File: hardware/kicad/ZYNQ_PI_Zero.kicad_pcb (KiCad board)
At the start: 6 copper layers, 65 x 30 mm, 111 parts, among them J1 HDMI_C_1.4, J201 Conn_02x05_Odd_Even, J202 Conn_01x04_Pin, J501 Conn_02x20_Counter_Clockwise, J701 USB_C_Receptacle_USB2.0_16P, J702 USB_C_Receptacle_USB2.0_16P, J703 USB_C_Receptacle_USB2.0_16P, J801 Micro_SD_Card, Q201 MMBT3904, U201 xc7z007sclg225, U301 MT41K256M16TW-107_P

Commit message: layout: finish dq0 & dq1 routing
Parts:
- removed C433: 10u, Capacitor_SMD:C_0805_2012Metric
- removed C435, C463, C464: 100n, Capacitor_SMD:C_0402_1005Metric
- removed C438: 100u, Capacitor_SMD:C_1206_3216Metric
- removed C443: 4u7, Capacitor_SMD:C_0603_1608Metric
- removed J1: HDMI_C_1.4, Projects:HDMI-SMD_A71-05H4-111N1
- removed J201: Conn_02x05_Odd_Even, Connector_PinSocket_2.54mm:PinSocket_2x05_P2.54mm_Vertical
- removed J702, J703: USB_C_Receptacle_USB2.0_16P, Connector_USB:USB_C_Receptacle_GCT_USB4105-xx-A_16P_TopMnt_Horizontal
- removed J801: Micro_SD_Card, Projects:TF-SMD_503398-1892
- added C301: 100n, Capacitor_SMD:C_0402_1005Metric, F.Cu at (116.2, 97.2)
- added C302: 100n, Capacitor_SMD:C_0402_1005Metric, F.Cu at (116.2, 98.1)
- added C303: 1u, Capacitor_SMD:C_0603_1608Metric, F.Cu at (105.5, 138.7)
- added C304: 1u, Capacitor_SMD:C_0603_1608Metric, F.Cu at (105.5, 141.2)
- added C305: 1u, Capacitor_SMD:C_0603_1608Metric, F.Cu at (105.5, 143.8)
- added C306: 1u, Capacitor_SMD:C_0603_1608Metric, F.Cu at (105.5, 146.3)
- added C307: 100n, Capacitor_SMD:C_0402_1005Metric, B.Cu at (117.2, 91.4)
- added C308: 1u, Capacitor_SMD:C_0603_1608Metric, F.Cu at (105.5, 148.8)
- added C309: 100n, Capacitor_SMD:C_0402_1005Metric, B.Cu at (118.9, 91.4)
- added C310: 100n, Capacitor_SMD:C_0402_1005Metric, B.Cu at (120.7, 91.4)
- added C311: 100n, Capacitor_SMD:C_0402_1005Metric, B.Cu at (116.3, 103.6)
- added C312: 100n, Capacitor_SMD:C_0402_1005Metric, B.Cu at (116.3, 105.2)
- added C313: 100n, Capacitor_SMD:C_0402_1005Metric, B.Cu at (147.8, 98.0)
- added C314: 100n, Capacitor_SMD:C_0402_1005Metric, B.Cu at (128.0, 105.2)
- added C315: 100n, Capacitor_SMD:C_0402_1005Metric, B.Cu at (116.7, 94.3)
- added C316: 100n, Capacitor_SMD:C_0402_1005Metric, B.Cu at (116.7, 96.0)
- added C317: 100n, Capacitor_SMD:C_0402_1005Metric, B.Cu at (116.7, 97.7)
- added C318: 100n, Capacitor_SMD:C_0402_1005Metric, B.Cu at (128.0, 103.6)
- added C701: 10u, Capacitor_SMD:C_0805_2012Metric, F.Cu at (296.2, 176.7)
- added C702: 100n, Capacitor_SMD:C_0402_1005Metric, F.Cu at (299.9, 176.2)
- added C901: 100n, Capacitor_SMD:C_0402_1005Metric, F.Cu at (267.1, 179.9)
- added D601: SS14, Diode_SMD:D_SMA, F.Cu at (303.0, 149.7)
- added D602: SS14, Diode_SMD:D_SMA, F.Cu at (303.0, 154.2)
- added D801: PL_LED, LED_SMD:LED_0603_1608Metric, F.Cu at (277.7, 172.3)
- added D902: PS_LED, LED_SMD:LED_0603_1608Metric, F.Cu at (267.7, 177.6)
- added F601: Polyfuse, Fuse:Fuse_0603_1608Metric, F.Cu at (296.0, 152.6)
- added FB701: 120OHM@100M, Inductor_SMD:L_0402_1005Metric, F.Cu at (310.1, 160.6)
- added IC401: TPS51206DSQR, Project:SON40P200X200X80-11N, F.Cu at (109.2, 99.2)
- added J203: Conn_02x03_Counter_Clockwise, Connector_PinHeader_2.00mm:PinHeader_2x03_P2.00mm_Vertical, F.Cu at (313.0, 106.3)
- added J401: USB_C_Receptacle_USB2.0_16P, Connector_USB:USB_C_Receptacle_GCT_USB4105-xx-A_16P_TopMnt_Horizontal, F.Cu at (281.0, 109.5)
- added J601: HDMI_C_1.4, Projects:HDMI-SMD_A71-05H4-111N1, F.Cu at (169.0, 102.0)
- added L401: CMLB041B-2R2MS, Project:IND_CMLB041B-1R0MS, F.Cu at (148.4, 145.4)
- added L402: CMLB041B-2R2MS, Project:IND_CMLB041B-1R0MS, F.Cu at (136.4, 145.4)
- added L403: CMLB041B-2R2MS, Project:IND_CMLB041B-1R0MS, F.Cu at (160.4, 145.4)
- added Q601: 2N7002, Package_TO_SOT_SMD:SOT-23, F.Cu at (296.4, 140.2)
- added Q602: 2N7002, Package_TO_SOT_SMD:SOT-23, F.Cu at (296.4, 144.7)
- added Q603: 2N7002, Package_TO_SOT_SMD:SOT-23, F.Cu at (296.4, 149.2)
- added R301: 4k7, Resistor_SMD:R_0402_1005Metric, B.Cu at (107.8, 106.5)
- added R302: 240R, Resistor_SMD:R_0402_1005Metric, B.Cu at (128.0, 102.4)
- added R303: 80R6, Resistor_SMD:R_0402_1005Metric, B.Cu at (146.2, 104.4)
- added R304: 40R2, Resistor_SMD:R_0402_1005Metric, B.Cu at (107.8, 103.5)
- added R305: 40R2, Resistor_SMD:R_0402_1005Metric, B.Cu at (107.8, 109.5)
- added R306: 40R2, Resistor_SMD:R_0402_1005Metric, B.Cu at (107.8, 104.5)
- added R307: 40R2, Resistor_SMD:R_0402_1005Metric, B.Cu at (110.0, 104.5)
- added R308: 40R2, Resistor_SMD:R_0402_1005Metric, B.Cu at (110.0, 110.5)
- added R309: 40R2, Resistor_SMD:R_0402_1005Metric, B.Cu at (110.0, 105.5)
- added R310: 40R2, Resistor_SMD:R_0402_1005Metric, B.Cu at (107.8, 111.5)
- added R311: 40R2, Resistor_SMD:R_0402_1005Metric, B.Cu at (107.8, 105.5)
- added R312: 40R2, Resistor_SMD:R_0402_1005Metric, B.Cu at (110.0, 112.5)
- added R313: 40R2, Resistor_SMD:R_0402_1005Metric, B.Cu at (110.0, 106.5)
- added R314: 40R2, Resistor_SMD:R_0402_1005Metric, B.Cu at (110.0, 108.5)
- added R315: 40R2, Resistor_SMD:R_0402_1005Metric, B.Cu at (107.8, 110.5)
- added R316: 40R2, Resistor_SMD:R_0402_1005Metric, B.Cu at (107.8, 108.5)
- added R317: 40R2, Resistor_SMD:R_0402_1005Metric, B.Cu at (110.0, 107.5)
- added R318: 40R2, Resistor_SMD:R_0402_1005Metric, B.Cu at (110.0, 111.5)
- added R319: 40R2, Resistor_SMD:R_0402_1005Metric, B.Cu at (110.0, 103.5)
- added R320: 40R2, Resistor_SMD:R_0402_1005Metric, B.Cu at (110.0, 109.5)
- added R321: 40R2, Resistor_SMD:R_0402_1005Metric, B.Cu at (107.8, 102.5)
- added R322: 40R2, Resistor_SMD:R_0402_1005Metric, B.Cu at (110.0, 102.5)
- added R323: 40R2, Resistor_SMD:R_0402_1005Metric, B.Cu at (110.0, 101.5)
- added R324: 40R2, Resistor_SMD:R_0402_1005Metric, B.Cu at (107.8, 101.5)
- added R325: 40R2, Resistor_SMD:R_0402_1005Metric, B.Cu at (110.0, 100.5)
- added R326: 40R2, Resistor_SMD:R_0402_1005Metric, B.Cu at (107.8, 100.5)
- added R327: 40R2, Resistor_SMD:R_0402_1005Metric, B.Cu at (107.8, 107.5)
- added R328: 80R6, Resistor_SMD:R_0402_1005Metric, B.Cu at (145.8, 100.9)
- added R329: 80R6, Resistor_SMD:R_0402_1005Metric, B.Cu at (146.5, 99.2)
- added R410: 18k7, Resistor_SMD:R_0402_1005Metric, F.Cu at (158.9, 140.7)
- added R411: 15k, Resistor_SMD:R_0402_1005Metric, F.Cu at (157.7, 140.7)
- added R601: 0R, Resistor_SMD:R_0402_1005Metric, F.Cu at (308.4, 148.4)
- added R602: 0R, Resistor_SMD:R_0402_1005Metric, F.Cu at (308.4, 150.4)
- added R603: 4k7, Resistor_SMD:R_0402_1005Metric, F.Cu at (308.4, 152.4)
- added R604: 4k7, Resistor_SMD:R_0402_1005Metric, F.Cu at (311.3, 148.4)
- added R605: 4k7, Resistor_SMD:R_0402_1005Metric, F.Cu at (311.3, 150.4)
- added R606: 4k7, Resistor_SMD:R_0402_1005Metric, F.Cu at (311.3, 152.4)
- added R607: 27k, Resistor_SMD:R_0603_1608Metric, F.Cu at (296.0, 155.1)
- added R608: 10k, Resistor_SMD:R_0402_1005Metric, F.Cu at (314.2, 148.4)
- added R609: 10k, Resistor_SMD:R_0402_1005Metric, F.Cu at (314.2, 150.4)
- added R610: 4k7, Resistor_SMD:R_0402_1005Metric, F.Cu at (314.2, 152.4)
- added R701: 47k, Resistor_SMD:R_0402_1005Metric, F.Cu at (310.1, 162.6)
- added R702: 47k, Resistor_SMD:R_0402_1005Metric, F.Cu at (310.1, 164.6)
- added R703: 47k, Resistor_SMD:R_0402_1005Metric, F.Cu at (310.1, 166.6)
- added R704: 47k, Resistor_SMD:R_0402_1005Metric, F.Cu at (310.1, 168.6)
- added R705: 47k, Resistor_SMD:R_0402_1005Metric, F.Cu at (310.1, 170.6)
- added R801: 10k, Resistor_SMD:R_0402_1005Metric, F.Cu at (274.2, 172.0)
- added R802: 100R, Resistor_SMD:R_0402_1005Metric, F.Cu at (274.2, 174.0)
- added R803: 1k, Resistor_SMD:R_0402_1005Metric, F.Cu at (274.2, 176.0)
- added R901: 33R, Resistor_SMD:R_0402_1005Metric, F.Cu at (258.8, 166.8)
- added R902: 33R, Resistor_SMD:R_0402_1005Metric, F.Cu at (258.8, 168.8)
- added R903: 4k7, Resistor_SMD:R_0402_1005Metric, F.Cu at (258.8, 170.8)
- added R904: 100R, Resistor_SMD:R_0402_1005Metric, F.Cu at (258.8, 172.8)
- added R905: 10k, Resistor_SMD:R_0402_1005Metric, F.Cu at (258.8, 174.8)
- added R906: 10k, Resistor_SMD:R_0402_1005Metric, F.Cu at (258.8, 176.7)
- added R907: 100R, Resistor_SMD:R_0402_1005Metric, F.Cu at (258.8, 178.7)
- added R908: 1k, Resistor_SMD:R_0402_1005Metric, F.Cu at (258.8, 180.7)
- added SW801: PL_KEY, Button_Switch_SMD:SW_Tactile_SPST_NO_Straight_CK_PTS636Sx25SMTRLFS, F.Cu at (278.1, 168.4)
- added SW901: RESET, Button_Switch_SMD:SW_Tactile_SPST_NO_Straight_CK_PTS636Sx25SMTRLFS, F.Cu at (265.5, 168.4)
- added SW902: PS_KEY, Button_Switch_SMD:SW_Tactile_SPST_NO_Straight_CK_PTS636Sx25SMTRLFS, F.Cu at (265.5, 173.7)
- added U202: W25Q128JVS, Package_SO:SOIC-8_5.3x5.3mm_P1.27mm, F.Cu at (300.1, 123.8)
- added U401: TPS62130ARGTR, Project:QFN50P300X300X100-17N-D, F.Cu at (143.4, 143.9)
- added U402: TPS62130ARGTR, Project:QFN50P300X300X100-17N-D, F.Cu at (131.4, 143.9)
- added U403: SPX3819M5-L-3-3, Project:SPX3819M5-L-3-3, F.Cu at (189.1, 143.6)
- added U405: TPS62130ARGTR, Project:QFN50P300X300X100-17N-D, F.Cu at (155.4, 143.9)
- added U601: TPD4E05U06DQA, Package_SON:USON-10_2.5x1.0mm_P0.5mm, F.Cu at (308.4, 155.6)
- added U602: TPD4E05U06DQA, Package_SON:USON-10_2.5x1.0mm_P0.5mm, F.Cu at (311.3, 155.6)
- added U901: 33.3333MHz, Oscillator:Oscillator_SMD_SeikoEpson_SG8002CE-4Pin_3.2x2.5mm, F.Cu at (263.0, 178.7)
- C201, C202, C429, C432, C447, C449, C451, C457, C459, C460, FB201, FB401, R204, R205: moved to B.Cu
- C407, C426: value 10u -> 22u
- C408: value 470n -> 22u; footprint Capacitor_SMD:C_0402_1005Metric -> Capacitor_SMD:C_0805_2012Metric
- C410: value 22u -> 10u; footprint Capacitor_SMD:C_0805_2012Metric -> Capacitor_SMD:C_0603_1608Metric; moved to B.Cu
- C411: value 22u -> 10u
- C413, C422, C454: value 10u -> 470n; footprint Capacitor_SMD:C_0805_2012Metric -> Capacitor_SMD:C_0402_1005Metric; moved to B.Cu
- C415: value 10u -> 100n; footprint Capacitor_SMD:C_0805_2012Metric -> Capacitor_SMD:C_0402_1005Metric
- C418: value 100u -> 10u; footprint Capacitor_SMD:C_1206_3216Metric -> Capacitor_SMD:C_0805_2012Metric
- C419, C425: value 10u -> 4u7; footprint Capacitor_SMD:C_0805_2012Metric -> Capacitor_SMD:C_0603_1608Metric
- C420, C424, C431, C452: value 470n -> 10u; footprint Capacitor_SMD:C_0402_1005Metric -> Capacitor_SMD:C_0805_2012Metric
- C421: value 4u7 -> 10u; footprint Capacitor_SMD:C_0603_1608Metric -> Capacitor_SMD:C_0805_2012Metric
- C427: value 4u7 -> 470n; footprint Capacitor_SMD:C_0603_1608Metric -> Capacitor_SMD:C_0402_1005Metric
- C428: value 22u -> 4u7; footprint Capacitor_SMD:C_0805_2012Metric -> Capacitor_SMD:C_0603_1608Metric
- C430, C442, C446, C450, C455, C458: value 4u7 -> 470n; footprint Capacitor_SMD:C_0603_1608Metric -> Capacitor_SMD:C_0402_1005Metric; moved to B.Cu
- C434: value 470n -> 100u; footprint Capacitor_SMD:C_0402_1005Metric -> Capacitor_SMD:C_1206_3216Metric
- C437: value 100u -> 4u7; footprint Capacitor_SMD:C_1206_3216Metric -> Capacitor_SMD:C_0603_1608Metric
- C440: value 100n -> 4u7; footprint Capacitor_SMD:C_0402_1005Metric -> Capacitor_SMD:C_0603_1608Metric
- C444, C448, C453, C456: value 470n -> 4u7; footprint Capacitor_SMD:C_0402_1005Metric -> Capacitor_SMD:C_0603_1608Metric
- C445: value 100n -> 470n; moved to B.Cu
- C461, C462: value 470n -> 100n; moved to B.Cu
- J701: value USB_C_Receptacle_USB2.0_16P -> Micro_SD_Card; footprint Connector_USB:USB_C_Receptacle_GCT_USB4105-xx-A_16P_TopMnt_Horizontal -> Projects:TF-SMD_503398-1892
- R207: value 470R -> 10k
- R401, R402: value 100k -> 5k1
- R403: value 49.9k -> 100k
- R404: value 200k -> 100k
- R405: value 13k -> 49.9k
- R406: value 15k -> 200k
- R407: value 100k -> 13k
- R408: value 18k7 -> 15k
- R409: value 15k -> 100k
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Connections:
- C201 pad 1: Net-(C201-Pad1) -> Net-(U201A-VCCADC_0)
- C407 pad 1: Net-(C407-Pad1) -> +1V0
- C408 pad 1: Net-(C407-Pad1) -> +1V5
- C410 pad 1: +1V0 -> Net-(U201G-VCCPLL)
- C411 pad 1: +1V5 -> +5V
- C412 pad 1: +5V -> +1V5
- C413 pad 1: +1V5 -> Net-(U201G-VCCPLL)
- C418 pad 1: +VCCIO_34 -> +3V3
- C419 pad 1: +3V3 -> +1V8
- C420 pad 1: +VCCIO_34 -> +1V0
- C421 pad 1: +1V8 -> +DDRVTT
- C422 pad 1: +1V0 -> +1V8
- C423 pad 1: +DDRVTT -> +1V0
- C424 pad 1: +1V8 -> +DDRVTT
- C426 pad 1: +DDRVTT -> +1V8
- C427 pad 1: +1V0 -> +VTTREF
- C428 pad 1: +1V8 -> +1V0
- C429 pad 1: +VTTREF -> +1V0
- C431 pad 1: +1V0 -> +3V3
- C434 pad 1: +1V0 -> +3V3
- C436 pad 1: +VCCIO_34 -> +1V5
- C437 pad 1: +VCCIO_35 -> +3V3
- C440 pad 1: +1V0 -> +3V3
- C441 pad 1: +VCCIO_34 -> +1V5
- C442 pad 1: +VCCIO_35 -> +3V3
- C444 pad 1: +3V3 -> +1V0
- C445 pad 1: +1V0 -> +3V3
- C446 pad 1: +1V0 -> +3V3
- C447 pad 1: +VCCIO_34 -> +1V5
- C448 pad 1: +VCCIO_35 -> +1V0
- C449 pad 1: +1V5 -> +3V3
- C450 pad 1: +1V0 -> +3V3
- C451 pad 1: +VCCIO_34 -> +1V5
- C452 pad 1: +VCCIO_35 -> +1V8
- C453 pad 1: +1V5 -> +1V8
- C454 pad 1: +1V8 -> +1V0
- C455 pad 1: +1V8 -> +1V5
- C456 pad 1: +1V0 -> +1V8
- C457 pad 1: +1V5 -> +1V8
- C458 pad 1: +1V8 -> +1V0
- C459 pad 1: +1V8 -> +1V5
- C460 pad 1: +1V0 -> +1V8
- C461 pad 1: +1V5 -> +1V8
- C462 pad 1: +1V8 -> +1V0
- FB201 pad 1: Net-(C201-Pad1) -> Net-(U201A-VCCADC_0)
- FB401 pad 1: Net-(C407-Pad1) -> Net-(U201G-VCCPLL)
- J501 pad 1: unconnected-(J501-Pin_1-Pad1) -> UART_TX
- J501 pad 2: unconnected-(J501-Pin_2-Pad2) -> UART_RX
- R208 pad 1: +3V3 -> GND
- R401 pad 1: +5V -> Net-(J401-CC2)
- R401 pad 2: /POWER/1V0_PG -> GND
- R402 pad 1: +5V -> Net-(J401-CC1)
- R402 pad 2: /POWER/1V5_PG -> GND
- R403 pad 1: +1V0 -> +5V
- R403 pad 2: Net-(U401-FB) (its old number) -> /POWER/1V0_PG
- R404 pad 1: Net-(U401-FB) (its old number) -> +5V
- R404 pad 2: GND -> /POWER/1V5_PG
- R405 pad 1: +1V5 -> +1V0
- R407 pad 1: +5V -> +1V5
- R407 pad 2: /POWER/1V8_PG -> Net-(U402-FB)
- R408 pad 1: +1V8 -> Net-(U402-FB)
- R408 pad 2: Net-(U405-FB) -> GND
- R409 pad 1: Net-(U405-FB) -> +5V
- R409 pad 2: GND -> /POWER/1V8_PG
- U201 pad A1: Net-(U201G-GND[31]-PadA1) -> GND
- U201 pad A10: unconnected-(U201D-PS_MIO6_500-PadA10) -> QSPI_CLK
- U201 pad A11: Net-(U201G-GND[31]-PadA1) -> GND
- U201 pad A2: unconnected-(U201F-PS_DDR_DQ1_502-PadA2) -> /DDR/DDR_D1
- U201 pad A3: unconnected-(U201F-PS_DDR_DQ7_502-PadA3) -> /DDR/DDR_D7
- U201 pad A4: unconnected-(U201F-PS_DDR_DQ5_502-PadA4) -> /DDR/DDR_D5
- U201 pad A5: unconnected-(U201D-PS_MIO1_500-PadA5) -> QSPI_CS
- U201 pad A6: Net-(U201D-VCCO_MIO0_500[2]-PadA6) -> +3V3
- U201 pad A7: unconnected-(U201D-PS_MIO3_500-PadA7) -> QSPI_D1
- U201 pad A8: unconnected-(U201D-PS_MIO2_500-PadA8) -> QSPI_D0
- U201 pad A9: unconnected-(U201D-PS_MIO5_500-PadA9) -> QSPI_D3_PS_MIO5
- U201 pad B1: unconnected-(U201F-PS_DDR_DM0_502-PadB1) -> /DDR/DDR_DM0
- U201 pad B10: unconnected-(U201D-PS_MIO11_500-PadB10) -> SD_CMD
- U201 pad B11: unconnected-(U201E-PS_SRST_B_501-PadB11) -> PS_SRST_B
- U201 pad B12: unconnected-(U201E-PS_MIO48_501-PadB12) -> UART_TX
- U201 pad B13: Net-(U201E-VCCO_MIO1_501[3]-PadB13) -> +3V3
- U201 pad B2: unconnected-(U201F-PS_DDR_DQS_N0_502-PadB2) -> /DDR/DDR_DQS0_N
- U201 pad B3: Net-(U201F-VCCO_DDR_502[6]-PadB3) -> +1V5
- U201 pad B4: unconnected-(U201F-PS_DDR_DQ4_502-PadB4) -> /DDR/DDR_D4
- U201 pad B5: unconnected-(U201D-PS_MIO9_500-PadB5) -> PS_LED
- U201 pad B6: unconnected-(U201D-PS_MIO8_500-PadB6) -> PS_MIO8
- U201 pad B7: unconnected-(U201D-PS_MIO12_500-PadB7) -> Net-(U201D-PS_MIO12_500)
- U201 pad B8: Net-(U201G-GND[31]-PadA1) -> GND
- U201 pad B9: unconnected-(U201D-PS_MIO14_500-PadB9) -> SD_DATA2
- U201 pad C1: unconnected-(U201F-PS_DDR_DQ3_502-PadC1) -> /DDR/DDR_D3
- U201 pad C10: Net-(U201E-VCCO_MIO1_501[3]-PadB13) -> +3V3
- U201 pad C15: Net-(U201G-GND[31]-PadA1) -> GND
- U201 pad C2: unconnected-(U201F-PS_DDR_DQS_P0_502-PadC2) -> /DDR/DDR_DQS0_P
- U201 pad C3: unconnected-(U201F-PS_DDR_DQ6_502-PadC3) -> /DDR/DDR_D6
- U201 pad C4: unconnected-(U201F-PS_DDR_DQ2_502-PadC4) -> /DDR/DDR_D2
- U201 pad C5: Net-(U201G-GND[31]-PadA1) -> GND
- U201 pad C6: unconnected-(U201D-PS_MIO13_500-PadC6) -> SD_DATA1
- U201 pad C7: unconnected-(U201D-PS_CLK_500-PadC7) -> Net-(U201D-PS_CLK_500)
- U201 pad C8: unconnected-(U201D-PS_MIO4_500-PadC8) -> QSPI_D2_PS_MIO4
- U201 pad C9: unconnected-(U201D-PS_POR_B_500-PadC9) -> SYS_RESET_N
- U201 pad D1: unconnected-(U201F-PS_DDR_DQ9_502-PadD1) -> /DDR/DDR_D9
- U201 pad D10: unconnected-(U201D-PS_MIO15_500-PadD10) -> SD_DATA3
- U201 pad D12: Net-(U201G-GND[31]-PadA1) -> GND
- U201 pad D13: unconnected-(U201E-PS_MIO49_501-PadD13) -> UART_RX
- U201 pad D2: Net-(U201G-GND[31]-PadA1) -> GND
- U201 pad D3: unconnected-(U201F-PS_DDR_DM1_502-PadD3) -> /DDR/DDR_DM1
- U201 pad D4: unconnected-(U201F-PS_DDR_DQ0_502-PadD4) -> /DDR/DDR_D0
- U201 pad D5: unconnected-(U201A-INIT_B_0-PadD5) -> /BANK0/INIT_B
- U201 pad D6: unconnected-(U201D-PS_MIO10_500-PadD6) -> SD_DATA0
- U201 pad D7: Net-(U201D-VCCO_MIO0_500[2]-PadA6) -> +3V3
- U201 pad D8: unconnected-(U201D-PS_MIO0_500-PadD8) -> PS_KEY
- U201 pad D9: unconnected-(U201D-PS_MIO7_500-PadD9) -> PS_MIO7
- U201 pad E1: unconnected-(U201F-PS_DDR_DQ8_502-PadE1) -> /DDR/DDR_D8
- U201 pad E10: Net-(U201G-VCCINT[5]-PadE10) -> +1V0
- U201 pad E11: unconnected-(U201C-IO_L2P_T0_AD8P_35-PadE11) -> HDMI_D0_P
- U201 pad E12: unconnected-(U201C-IO_L2N_T0_AD8N_35-PadE12) -> HDMI_D0_N
- U201 pad E13: unconnected-(U201C-IO_L1N_T0_AD0N_35-PadE13) -> HDMI_CLK_N
- U201 pad E14: Net-(U201E-VCCO_MIO1_501[3]-PadB13) -> +3V3
- U201 pad E2: unconnected-(U201F-PS_DDR_DQ10_502-PadE2) -> /DDR/DDR_D10
- U201 pad E3: unconnected-(U201F-PS_DDR_DQ11_502-PadE3) -> /DDR/DDR_D11
- U201 pad E4: Net-(U201F-VCCO_DDR_502[6]-PadB3) -> +1V5
- U201 pad E5: Net-(U201G-GND[31]-PadA1) -> GND
- U201 pad E6: unconnected-(U201A-VCCBATT_0-PadE6) -> +1V8
- U201 pad E7: Net-(U201G-GND[31]-PadA1) -> GND
- U201 pad E8: unconnected-(U201A-RSVDGND-PadE8) -> GND
- U201 pad E9: Net-(U201G-GND[31]-PadA1) -> GND
- U201 pad F1: Net-(U201F-VCCO_DDR_502[6]-PadB3) -> +1V5
- U201 pad F10: Net-(U201G-GND[31]-PadA1) -> GND
- U201 pad F11: Net-(U201C-VCCO_35[2]-PadF11) -> +3V3
- U201 pad F12: unconnected-(U201C-IO_L1P_T0_AD0P_35-PadF12) -> HDMI_CLK_P
- U201 pad F13: unconnected-(U201C-IO_L3P_T0_DQS_AD1P_35-PadF13) -> HDMI_D1_P
- U201 pad F14: unconnected-(U201C-IO_L3N_T0_DQS_AD1N_35-PadF14) -> HDMI_D1_N
- U201 pad F15: unconnected-(U201C-IO_L5N_T0_AD9N_35-PadF15) -> HDMI_D2_N
- U201 pad F2: unconnected-(U201F-PS_DDR_DQS_N1_502-PadF2) -> /DDR/DDR_DQS1_N
- U201 pad F3: unconnected-(U201F-PS_DDR_DQ12_502-PadF3) -> /DDR/DDR_D12
- U201 pad F4: unconnected-(U201F-PS_DDR_VREF0_502-PadF4) -> +VTTREF
- U201 pad F5: unconnected-(U201G-VCCPLL-PadF5) -> Net-(U201G-VCCPLL)
- U201 pad F6: unconnected-(U201A-CFGBVS_0-PadF6) -> +3V3
- U201 pad F7: unconnected-(U201A-VCCADC_0-PadF7) -> Net-(U201A-VCCADC_0)
- U201 pad F8: unconnected-(U201A-GNDADC_0-PadF8) -> GND
- U201 pad F9: Net-(U201G-VCCINT[5]-PadE10) -> +1V0
- U201 pad G1: unconnected-(U201F-PS_DDR_DQ13_502-PadG1) -> /DDR/DDR_D13
- U201 pad G10: Net-(U201G-VCCINT[5]-PadE10) -> +1V0
- U201 pad G11: unconnected-(U201B-IO_L1P_T0_34-PadG11) -> HDMI_HPD_N_3V3
- U201 pad G12: unconnected-(U201B-IO_L2P_T0_34-PadG12) -> HDMI_DDC_SDA_3V3
- U201 pad G13: Net-(U201G-GND[31]-PadA1) -> GND
- U201 pad G15: unconnected-(U201C-IO_L5P_T0_AD9P_35-PadG15) -> HDMI_D2_P
- U201 pad G2: unconnected-(U201F-PS_DDR_DQS_P1_502-PadG2) -> /DDR/DDR_DQS1_P
- U201 pad G3: Net-(U201G-GND[31]-PadA1) -> GND
- U201 pad G4: unconnected-(U201A-RSVDVCC1-PadG4) -> +3V3
- U201 pad G5: Net-(U201G-GND[31]-PadA1) -> GND
- U201 pad G6: Net-(U201G-VCCPINT[3]-PadG6) -> +1V0
- U201 pad G7: unconnected-(U201A-VP_0-PadG7) -> GND
- U201 pad G8: unconnected-(U201A-VREFN_0-PadG8) -> GND
- U201 pad G9: unconnected-(U201A-TCK_0-PadG9) -> TCK
- U201 pad H1: unconnected-(U201F-PS_DDR_DQ14_502-PadH1) -> /DDR/DDR_D14
- U201 pad H10: Net-(U201G-GND[31]-PadA1) -> GND
- U201 pad H13: unconnected-(U201B-IO_L2N_T0_34-PadH13) -> HDMI_DDC_SCL_3V3
- U201 pad H15: Net-(U201C-VCCO_35[2]-PadF11) -> +3V3
- U201 pad H2: unconnected-(U201F-PS_DDR_DQ15_502-PadH2) -> /DDR/DDR_D15
- U201 pad H3: unconnected-(U201F-PS_DDR_VRP_502-PadH3) -> Net-(U201F-PS_DDR_VRP_502)
- U201 pad H4: unconnected-(U201A-RSVDVCC3-PadH4) -> +3V3
- U201 pad H5: Net-(U201G-VCCPINT[3]-PadG6) -> +1V0
- U201 pad H6: Net-(U201G-GND[31]-PadA1) -> GND
- U201 pad H7: unconnected-(U201A-VREFP_0-PadH7) -> GND
- U201 pad H8: unconnected-(U201A-VN_0-PadH8) -> GND
- U201 pad H9: Net-(U201G-VCCAUX[3]-PadH9) -> +1V8
- U201 pad J1: unconnected-(U201F-PS_DDR_A10_502-PadJ1) -> /DDR/DDR_A10
- U201 pad J10: Net-(U201G-VCCINT[5]-PadE10) -> +1V0
- U201 pad J12: Net-(U201B-VCCO_34[5]-PadJ12) -> +3V3
- U201 pad J14: unconnected-(U201B-IO_L5N_T0_34-PadJ14) -> PL_LED
- U201 pad J15: unconnected-(U201B-IO_L4P_T0_34-PadJ15) -> PL_KEY
- U201 pad J2: Net-(U201F-VCCO_DDR_502[6]-PadB3) -> +1V5
- U201 pad J3: unconnected-(U201F-PS_DDR_VRN_502-PadJ3) -> Net-(U201F-PS_DDR_VRN_502)
- U201 pad J4: unconnected-(U201A-RSVDVCC2-PadJ4) -> +3V3
- U201 pad J5: Net-(U201G-GND[31]-PadA1) -> GND
- U201 pad J6: Net-(U201G-VCCPAUX[2]-PadJ6) -> +1V8
- U201 pad J7: unconnected-(U201A-DXP_0-PadJ7) -> GND
- U201 pad J8: Net-(U201G-VCCAUX[3]-PadH9) -> +1V8
- U201 pad J9: Net-(U201G-GND[31]-PadA1) -> GND
- U201 pad K1: unconnected-(U201F-PS_DDR_A14_502-PadK1) -> /DDR/DDR_A14
- U201 pad K10: Net-(U201G-GND[31]-PadA1) -> GND
- U201 pad K14: Net-(U201G-GND[31]-PadA1) -> GND
- U201 pad K2: unconnected-(U201F-PS_DDR_A13_502-PadK2) -> /DDR/DDR_A13
- U201 pad K3: unconnected-(U201F-PS_DDR_ODT_502-PadK3) -> /DDR/DDR_ODT
- U201 pad K4: Net-(U201G-GND[31]-PadA1) -> GND
- U201 pad K5: Net-(U201G-VCCPINT[3]-PadG6) -> +1V0
- U201 pad K6: unconnected-(U201A-PROGRAM_B_0-PadK6) -> /BANK0/PROGRAM_B
- U201 pad K7: Net-(U201G-GND[31]-PadA1) -> GND
- U201 pad K8: unconnected-(U201A-VCCO_0-PadK8) -> +3V3
- U201 pad K9: Net-(U201G-VCCAUX[3]-PadH9) -> +1V8
- U201 pad L1: Net-(U201G-GND[31]-PadA1) -> GND
- U201 pad L10: Net-(U201G-VCCINT[5]-PadE10) -> +1V0
- U201 pad L11: Net-(U201G-GND[31]-PadA1) -> GND
- U201 pad L2: unconnected-(U201F-PS_DDR_A11_502-PadL2) -> /DDR/DDR_A11
- U201 pad L3: unconnected-(U201F-PS_DDR_CKE_502-PadL3) -> /DDR/DDR_CKE
- U201 pad L4: unconnected-(U201F-PS_DDR_DRST_B_502-PadL4) -> /DDR/DDR_~{RESET}
- U201 pad L5: Net-(U201G-GND[31]-PadA1) -> GND
- U201 pad L6: Net-(U201G-VCCPAUX[2]-PadJ6) -> +1V8
- U201 pad L7: unconnected-(U201A-TDI_0-PadL7) -> TDI
- U201 pad L8: unconnected-(U201A-TDO_0-PadL8) -> TDO
- U201 pad L9: unconnected-(U201A-TMS_0-PadL9) -> TMS
- U201 pad M1: unconnected-(U201F-PS_DDR_A2_502-PadM1) -> /DDR/DDR_A2
- U201 pad M13: Net-(U201B-VCCO_34[5]-PadJ12) -> +3V3
- U201 pad M2: unconnected-(U201F-PS_DDR_A12_502-PadM2) -> /DDR/DDR_A12
- U201 pad M3: Net-(U201F-VCCO_DDR_502[6]-PadB3) -> +1V5
- U201 pad M4: unconnected-(U201F-PS_DDR_A3_502-PadM4) -> /DDR/DDR_A3
- U201 pad M5: unconnected-(U201F-PS_DDR_A7_502-PadM5) -> /DDR/DDR_A7
- U201 pad M6: unconnected-(U201F-PS_DDR_BA0_502-PadM6) -> /DDR/DDR_BA0
- U201 pad M7: unconnected-(U201A-DONE_0-PadM7) -> DONE
- U201 pad M8: Net-(U201G-GND[31]-PadA1) -> GND
- U201 pad N1: unconnected-(U201F-PS_DDR_A1_502-PadN1) -> /DDR/DDR_A1
- U201 pad N10: Net-(U201B-VCCO_34[5]-PadJ12) -> +3V3
- U201 pad N15: Net-(U201G-GND[31]-PadA1) -> GND
- U201 pad N2: unconnected-(U201F-PS_DDR_CKN_502-PadN2) -> /DDR/DDR_CLK_N
- U201 pad N3: unconnected-(U201F-PS_DDR_CKP_502-PadN3) -> /DDR/DDR_CLK_P
- U201 pad N4: unconnected-(U201F-PS_DDR_A9_502-PadN4) -> /DDR/DDR_A9
- U201 pad N5: Net-(U201G-GND[31]-PadA1) -> GND
- U201 pad N6: unconnected-(U201F-PS_DDR_BA2_502-PadN6) -> /DDR/DDR_BA2
- U201 pad P1: unconnected-(U201F-PS_DDR_A0_502-PadP1) -> /DDR/DDR_A0
- U201 pad P12: Net-(U201G-GND[31]-PadA1) -> GND
- U201 pad P2: Net-(U201G-GND[31]-PadA1) -> GND
- U201 pad P3: unconnected-(U201F-PS_DDR_A4_502-PadP3) -> /DDR/DDR_A4
- U201 pad P4: unconnected-(U201F-PS_DDR_A5_502-PadP4) -> /DDR/DDR_A5
- U201 pad P5: unconnected-(U201F-PS_DDR_A6_502-PadP5) -> /DDR/DDR_A6
- U201 pad P6: unconnected-(U201F-PS_DDR_A8_502-PadP6) -> /DDR/DDR_A8
- U201 pad P7: Net-(U201B-VCCO_34[5]-PadJ12) -> +3V3
- U201 pad R1: unconnected-(U201F-PS_DDR_BA1_502-PadR1) -> /DDR/DDR_BA1
- U201 pad R14: Net-(U201B-VCCO_34[5]-PadJ12) -> +3V3
- U201 pad R2: unconnected-(U201F-PS_DDR_CS_B_502-PadR2) -> /DDR/DDR_~{CS}
- U201 pad R3: unconnected-(U201F-PS_DDR_WE_B_502-PadR3) -> /DDR/DDR_~{WE}
- U201 pad R4: Net-(U201F-VCCO_DDR_502[6]-PadB3) -> +1V5
- U201 pad R5: unconnected-(U201F-PS_DDR_CAS_B_502-PadR5) -> /DDR/DDR_~{CAS}
- U201 pad R6: unconnected-(U201F-PS_DDR_RAS_B_502-PadR6) -> /DDR/DDR_~{RAS}
- U201 pad R9: Net-(U201G-GND[31]-PadA1) -> GND
- U301 pad A1: VDDQ -> +1V5
- U301 pad A2: unconnected-(U301-DQ13-PadA2) -> /DDR/DDR_D12
- U301 pad A3: unconnected-(U301-DQ15-PadA3) -> /DDR/DDR_D11
- U301 pad A7: unconnected-(U301-DQ12-PadA7) -> /DDR/DDR_D13
- U301 pad A8: VDDQ -> +1V5
- U301 pad A9: VSS -> GND
- U301 pad B1: VSSQ -> GND
- U301 pad B2: VDD -> +1V5
- U301 pad B3: VSS -> GND
- U301 pad B7: unconnected-(U301-~{UDQS}-PadB7) -> /DDR/DDR_DQS1_N
- U301 pad B8: unconnected-(U301-DQ14-PadB8) -> /DDR/DDR_D15
- U301 pad B9: VSSQ -> GND
- U301 pad C1: VDDQ -> +1V5
- U301 pad C2: unconnected-(U301-DQ11-PadC2) -> /DDR/DDR_D9
- U301 pad C3: unconnected-(U301-DQ9-PadC3) -> /DDR/DDR_D10
- U301 pad C7: unconnected-(U301-UDQS-PadC7) -> /DDR/DDR_DQS1_P
- U301 pad C8: unconnected-(U301-DQ10-PadC8) -> /DDR/DDR_D14
- U301 pad C9: VDDQ -> +1V5
- U301 pad D1: VSSQ -> GND
- U301 pad D2: VDDQ -> +1V5
- U301 pad D3: unconnected-(U301-UDM-PadD3) -> /DDR/DDR_DM1
- U301 pad D7: unconnected-(U301-DQ8-PadD7) -> /DDR/DDR_D8
- U301 pad D8: VSSQ -> GND
- U301 pad D9: VDD -> +1V5
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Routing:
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- added copper zone on F.Cu, net +1V0
- added copper zone on In2.Cu, net +1V0
- added copper zone on F.Cu, net +1V5
- added copper zone on In2.Cu, net +1V5
- added copper zone on F.Cu, net +1V8
- added copper zone on In2.Cu, net +1V8
- added copper zone on In2.Cu, net +3V3
- added copper zone on F.Cu, net +5V
- added copper zone on F.Cu, net /POWER/1V0_SW
- added copper zone on F.Cu, net /POWER/1V5_SW
- added copper zone on F.Cu, net /POWER/1V8_SW
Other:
- board size 65 x 30 mm -> 85.4 x 54 mm
- copper layers 6 -> 4

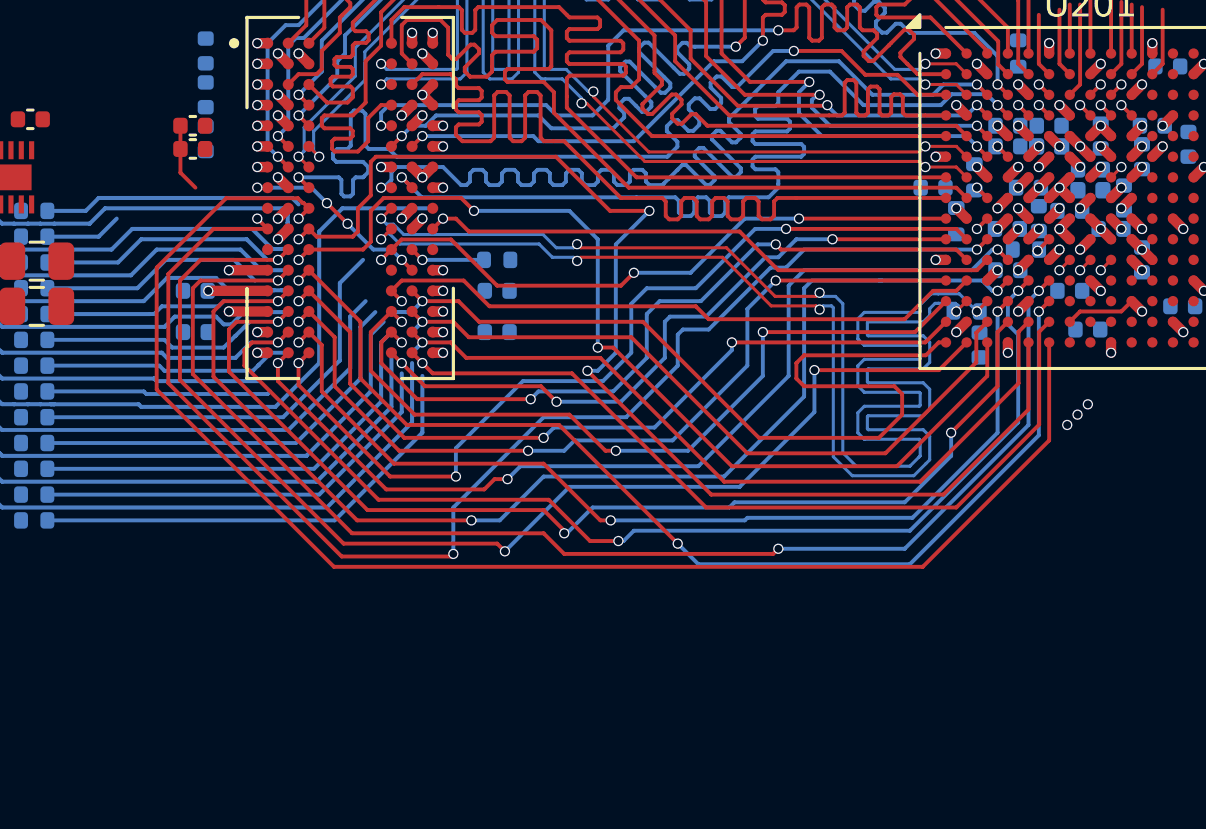
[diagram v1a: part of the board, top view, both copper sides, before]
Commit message: layout: finish ddr ctrl routing
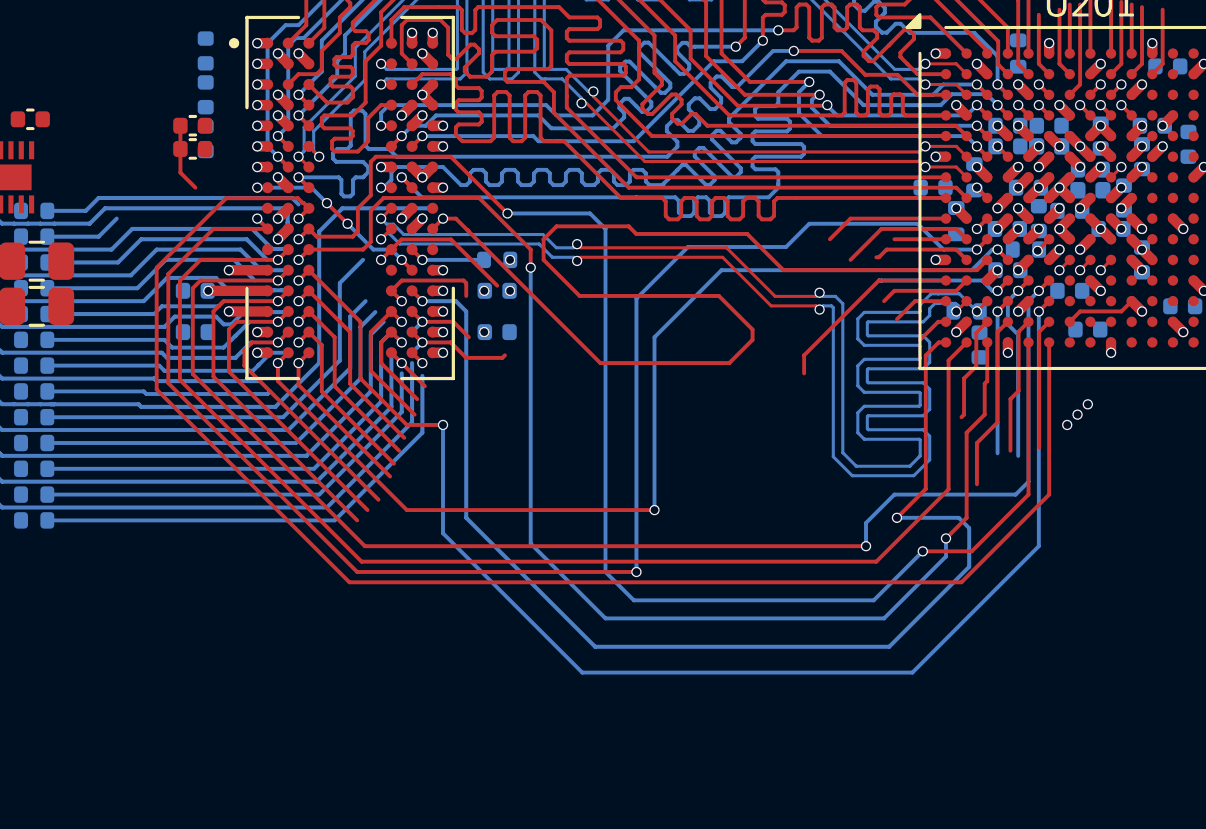
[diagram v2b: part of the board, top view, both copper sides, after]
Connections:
- R301 pad 1: /DDR/DDR_~{RESET} -> unconnected-(R301-Pad1)
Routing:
- net /DDR/DDR_A8: track 32.3 -> 5.61 mm
- net /DDR/DDR_A3: track 45.6 -> 19.0 mm, vias 3 -> 2
- net /DDR/DDR_A7: track 43.3 -> 17.2 mm, vias 3 -> 2
- net /DDR/DDR_A9: track 38.0 -> 13.1 mm, vias 3 -> 2
- net /DDR/DDR_A5: track 42.2 -> 18.6 mm, vias 3 -> 1
- net /DDR/DDR_A13: track 34.7 -> 11.6 mm, vias 3 -> 1
- net /DDR/DDR_A1: track 30.2 -> 7.79 mm, vias 3 -> 1
- net /DDR/DDR_A14: track 25.7 -> 3.84 mm, vias 3 -> 1
- net /DDR/DDR_A0: track 30.8 -> 9.09 mm, vias 3 -> 1
- net /DDR/DDR_CKE: track 22.7 -> 44.0 mm
- net /DDR/DDR_A11: track 28.9 -> 7.69 mm, vias 3 -> 1
- net /DDR/DDR_A6: track 30.6 -> 9.91 mm
- net /DDR/DDR_A4: track 28.0 -> 7.33 mm
- net /DDR/DDR_A2: track 32.6 -> 14.8 mm, vias 3 -> 1
- net /DDR/DDR_A12: track 24.3 -> 7.70 mm
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
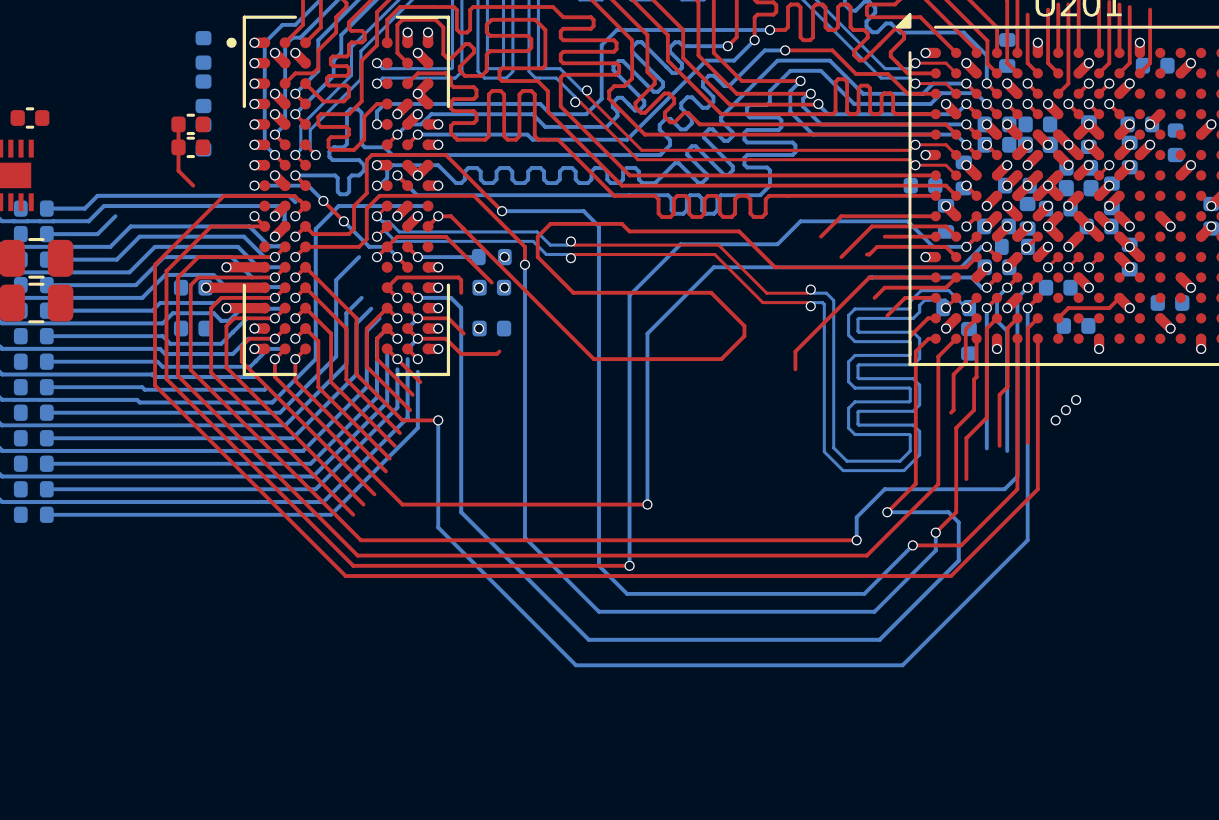
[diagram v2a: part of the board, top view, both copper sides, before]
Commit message: layout: vertical routing
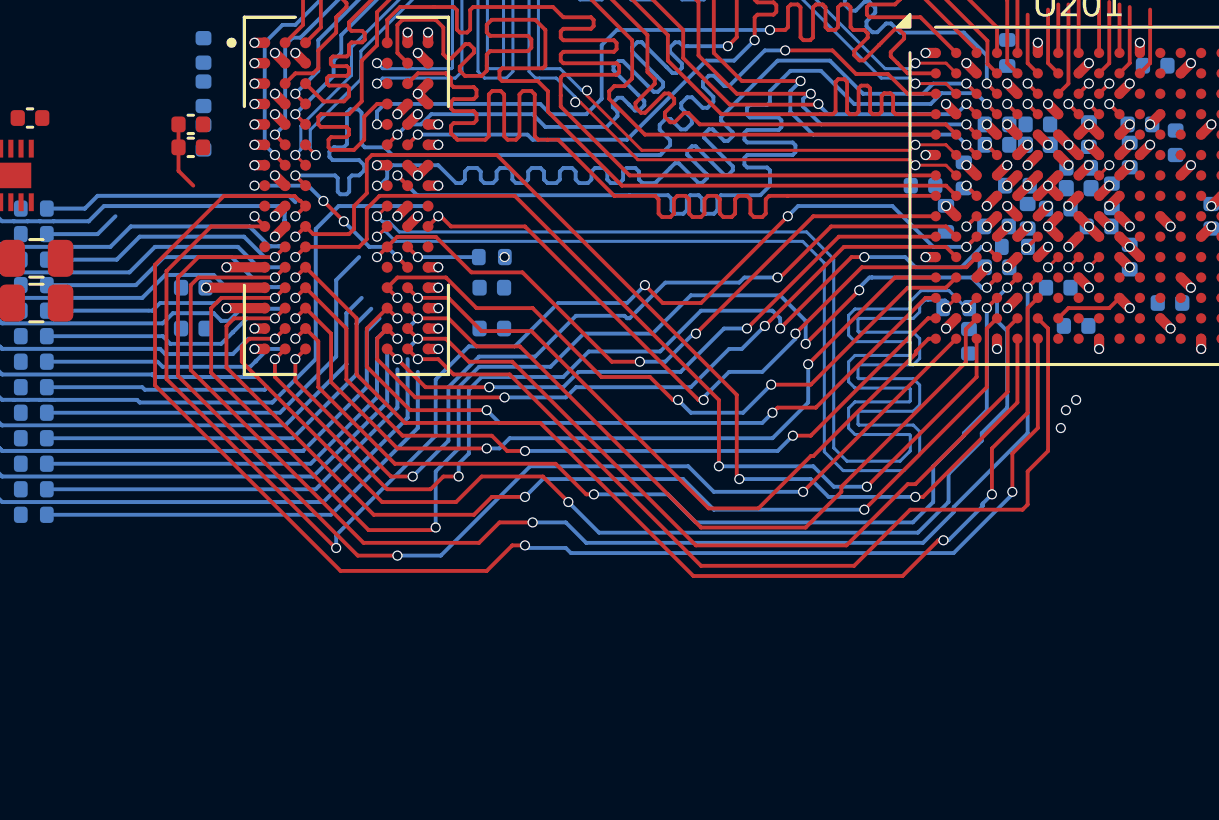
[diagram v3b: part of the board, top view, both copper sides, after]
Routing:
- net /DDR/DDR_A8: track 5.61 -> 36.6 mm
- net /DDR/DDR_A3: track 19.0 -> 48.5 mm, vias 2 -> 5
- net /DDR/DDR_A7: track 17.2 -> 44.6 mm, vias 2 -> 3
- net /DDR/DDR_A9: track 13.1 -> 38.7 mm, vias 2 -> 3
- net /DDR/DDR_A5: track 18.6 -> 42.3 mm, vias 1 -> 3
- net /DDR/DDR_A4: track 7.33 -> 30.7 mm
- net /DDR/DDR_A6: track 9.91 -> 33.1 mm
- net /DDR/DDR_A13: track 11.6 -> 34.4 mm, vias 1 -> 3
- net /DDR/DDR_A0: track 9.09 -> 31.2 mm, vias 1 -> 3
- net /DDR/DDR_A14: track 3.84 -> 24.6 mm, vias 1 -> 3
- net /DDR/DDR_A1: track 7.79 -> 28.4 mm, vias 1 -> 3
- net /DDR/DDR_A11: track 7.69 -> 27.9 mm, vias 1 -> 3
- net /DDR/DDR_A12: track 7.70 -> 27.4 mm, vias 1 -> 3
- net /DDR/DDR_BA1: track 45.5 -> 27.1 mm, vias 2 -> 1
- net /DDR/DDR_A2: track 14.8 -> 32.4 mm, vias 1 -> 3
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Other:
- board text added: "ADDR rail 1"
- board text added: "ADDR rail 2"
- board text added: "ADDR/CTRL MAIN BUS CHANNEL"
- board text added: "CLK corridor: route first, keep WE/CKE away"
- board text added: "CODEx DDR ADDR/CTRL GUIDE - User.Drawings"
- board text added: "CTRL/BA rail"
- board text added: "Do not tune inside BGA fields"
- board text added: "Do not use random vias; use the two via gates"
- board text added: "Keep CLK pair isolated; current 0.4mm rule will flag close ADDR/CTRL"
- board text added: "LENGTH TUNING ZONE: add U-shapes here only"
- board text added: "U201 escape: short fanout only"
- board text added: "U201 via gate"
- board text added: "U301 entry: no meanders"
- board text added: "U301 via gate"
- board text added: "flow: fanout -> via gate -> bus -> via gate -> entry"
- board text added: "tuning entry rail"

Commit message: finish basic ddr routing
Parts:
- removed J601: HDMI_C_1.4, Projects:HDMI-SMD_A71-05H4-111N1
- removed R801, R906: 10k, Resistor_SMD:R_0402_1005Metric
- removed R802, R907: 100R, Resistor_SMD:R_0402_1005Metric
- removed SW801: PL_KEY, Button_Switch_SMD:SW_Tactile_SPST_NO_Straight_CK_PTS636Sx25SMTRLFS
- removed SW902: PS_KEY, Button_Switch_SMD:SW_Tactile_SPST_NO_Straight_CK_PTS636Sx25SMTRLFS
- added J602: HDMI_A_1.4, Connector_Video:HDMI_A_Amphenol_10029449-x01xLF_Horizontal, F.Cu at (174.0, 100.0)
- C702, FB701, R701, R702, R703, R704, R705, R901: moved to B.Cu
- moved R705 216.8 mm to (114.4, 77.2), turned to 180 degrees
- moved R702 216.4 mm to (114.4, 72.2), turned to 180 degrees
- moved R704 215.4 mm to (114.4, 78.5), turned to 180 degrees
- moved R701 215.0 mm to (114.4, 73.5), turned to 180 degrees
- moved R703 214.1 mm to (114.4, 79.8), turned to 180 degrees
- moved FB701 213.2 mm to (114.4, 76.0)
- moved C702 211.4 mm to (114.4, 74.8), turned to 180 degrees
- moved C701 200.4 mm to (117.8, 85.5), turned to 180 degrees
- moved J202 177.2 mm to (144.2, 80.5), turned to 90 degrees
- moved C203 162.8 mm to (158.5, 81.2), turned to 90 degrees
- moved R210 161.4 mm to (155.5, 81.2), turned to -90 degrees
- moved R207 160.7 mm to (154.5, 81.2), turned to -90 degrees
- moved R209 159.9 mm to (156.5, 81.2), turned to -90 degrees
- moved R216 158.9 mm to (160.0, 84.8)
- moved R215 158.6 mm to (160.0, 83.7)
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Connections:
- U201 pad D8: PS_KEY -> unconnected-(U201D-PS_MIO0_500-PadD8)
- U201 pad E11: HDMI_D0_P -> unconnected-(U201C-IO_L2P_T0_AD8P_35-PadE11)
- U201 pad E12: HDMI_D0_N -> unconnected-(U201C-IO_L2N_T0_AD8N_35-PadE12)
- U201 pad E13: HDMI_CLK_N -> unconnected-(U201C-IO_L1N_T0_AD0N_35-PadE13)
- U201 pad F12: HDMI_CLK_P -> unconnected-(U201C-IO_L1P_T0_AD0P_35-PadF12)
- U201 pad F13: HDMI_D1_P -> unconnected-(U201C-IO_L3P_T0_DQS_AD1P_35-PadF13)
- U201 pad F14: HDMI_D1_N -> unconnected-(U201C-IO_L3N_T0_DQS_AD1N_35-PadF14)
- U201 pad F15: HDMI_D2_N -> unconnected-(U201C-IO_L5N_T0_AD9N_35-PadF15)
- U201 pad G14: unconnected-(U201B-IO_L3P_T0_DQS_PUDC_B_34-PadG14) -> PL_LED
- U201 pad G15: HDMI_D2_P -> unconnected-(U201C-IO_L5P_T0_AD9P_35-PadG15)
- U201 pad J14: PL_LED -> unconnected-(U201B-IO_L5N_T0_34-PadJ14)
- U201 pad J15: PL_KEY -> HDMI_D2_P
- U201 pad K15: unconnected-(U201B-IO_L4N_T0_34-PadK15) -> HDMI_D2_N
- U201 pad L15: unconnected-(U201B-IO_L8P_T1_34-PadL15) -> HDMI_D1_P
- U201 pad M15: unconnected-(U201B-IO_L8N_T1_34-PadM15) -> HDMI_D1_N
- U201 pad P15: unconnected-(U201B-IO_L15P_T2_DQS_34-PadP15) -> HDMI_D0_P
- U201 pad R12: unconnected-(U201B-IO_L17P_T2_34-PadR12) -> HDMI_CLK_N
- U201 pad R13: unconnected-(U201B-IO_L17N_T2_34-PadR13) -> HDMI_CLK_P
- U201 pad R15: unconnected-(U201B-IO_L15N_T2_DQS_34-PadR15) -> HDMI_D0_N
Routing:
- net SD_CMD: track 2.77 -> 84.0 mm, vias 0 -> 2
- net SD_DATA2: track 2.97 -> 73.1 mm, vias 0 -> 2
- net SD_DATA3: track 0.57 -> 69.4 mm, vias 1 -> 2
- net SD_CLK: track 0.00 -> 55.3 mm, vias 0 -> 1
- net SD_DATA1: track 0.57 -> 47.0 mm, vias 1 -> 2
- net SD_DATA0: track 0.57 -> 46.9 mm, vias 1 -> 2
- net /DDR/DDR_CKE: track 27.1 -> 60.4 mm, vias 3 -> 1
- net /DDR/DDR_BA1: track 27.1 -> 60.2 mm
- net /DDR/DDR_A14: track 24.6 -> 57.4 mm
- net /DDR/DDR_A12: track 27.4 -> 59.4 mm, vias 3 -> 1
- net /DDR/DDR_A10: track 26.6 -> 56.4 mm
- net /DDR/DDR_A11: track 27.9 -> 56.9 mm
- net /DDR/DDR_A4: track 30.7 -> 59.0 mm
- net /DDR/DDR_A1: track 28.4 -> 56.6 mm
- net /DDR/DDR_A0: track 31.2 -> 56.5 mm
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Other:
- board size 85.4 x 54 mm -> 85.4 x 68.3 mm

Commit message: pcb: complete FPGA and DDR BGA breakout
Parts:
- removed C303, C304, C305, C306, C308: 1u, Capacitor_SMD:C_0603_1608Metric
- removed C412, C421, C424: 10u, Capacitor_SMD:C_0805_2012Metric
- removed C415: 100n, Capacitor_SMD:C_0402_1005Metric
- removed C427: 470n, Capacitor_SMD:C_0402_1005Metric
- removed IC401: TPS51206DSQR, Project:SON40P200X200X80-11N
- removed R306, R307, R308, R309, R310, R311, R312, R313, R314, R315, R316, R317, R318, R319, R320, R321, R322, R323, R324, R325, R326, R327: 40R2, Resistor_SMD:R_0402_1005Metric
- R304, R305: value 40R2 -> 80R6
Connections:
- R304 pad 1: unconnected-(R304-Pad1) -> +1V5
- R304 pad 2: +DDRVTT -> +VTTREF
- R305 pad 1: unconnected-(R305-Pad1) -> +VTTREF
- R305 pad 2: +DDRVTT -> GND
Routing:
- net /DDR/DDR_CKE: track 60.4 -> 6.57 mm
- net /DDR/DDR_BA1: track 60.2 -> 6.76 mm, vias 1 -> 0
- net /DDR/DDR_A12: track 59.4 -> 9.73 mm
- net /DDR/DDR_A14: track 57.4 -> 8.70 mm, vias 3 -> 1
- net /DDR/DDR_A4: track 59.0 -> 10.4 mm, vias 1 -> 0
- net /DDR/DDR_A1: track 56.6 -> 8.70 mm, vias 3 -> 1
- net /DDR/DDR_A11: track 56.9 -> 9.25 mm, vias 3 -> 1
- net /DDR/DDR_~{CS}: track 57.0 -> 10.5 mm, vias 3 -> 1
- net /DDR/DDR_A10: track 56.4 -> 9.94 mm, vias 3 -> 0
- net /DDR/DDR_A2: track 57.1 -> 10.7 mm, vias 3 -> 0
- net /DDR/DDR_A8: track 60.0 -> 14.5 mm, vias 1 -> 0
- net /DDR/DDR_A6: track 58.1 -> 12.7 mm, vias 1 -> 0
- net /DDR/DDR_A0: track 56.5 -> 11.3 mm, vias 3 -> 0
- net /DDR/DDR_A13: track 56.6 -> 11.5 mm, vias 3 -> 0
- net /DDR/DDR_A3: track 54.2 -> 10.7 mm, vias 5 -> 2
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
